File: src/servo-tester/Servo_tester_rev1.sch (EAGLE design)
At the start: 19 parts, among them IC1 7806T

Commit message: Fixed discrepancy between brd and sch, corrected pulldowns
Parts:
- added R10, R7, R8, R9: 10M, adafruit:R-US_0204/5
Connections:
- new net 33V_PULLUP: JP3.6, JP4.2, JP5.2, JP6.2, JP7.2
- net BTN1: now also R7.1
- net BTN2: now also R8.2
- net BTN3: now also R9.2
- net BTN4: now also R10.2
- net GND: now also R10.1, R7.2, R8.1, R9.1; no longer JP4.2, JP5.2, JP6.2, JP7.2
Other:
- moved on the sheet: JP4, JP5, JP6, JP7

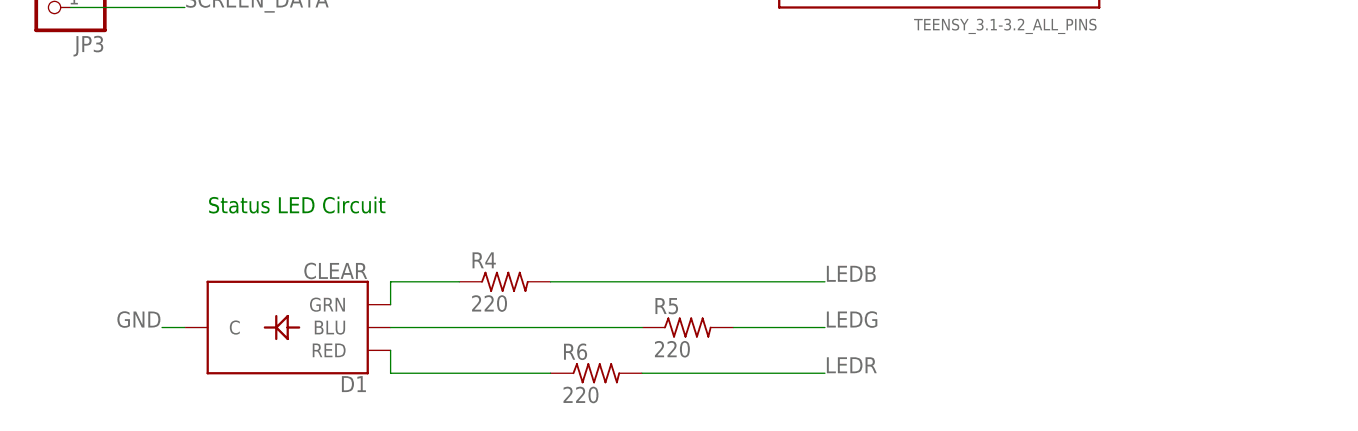
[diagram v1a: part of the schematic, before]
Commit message: fixed DRCs and made smaller
also added copper fill
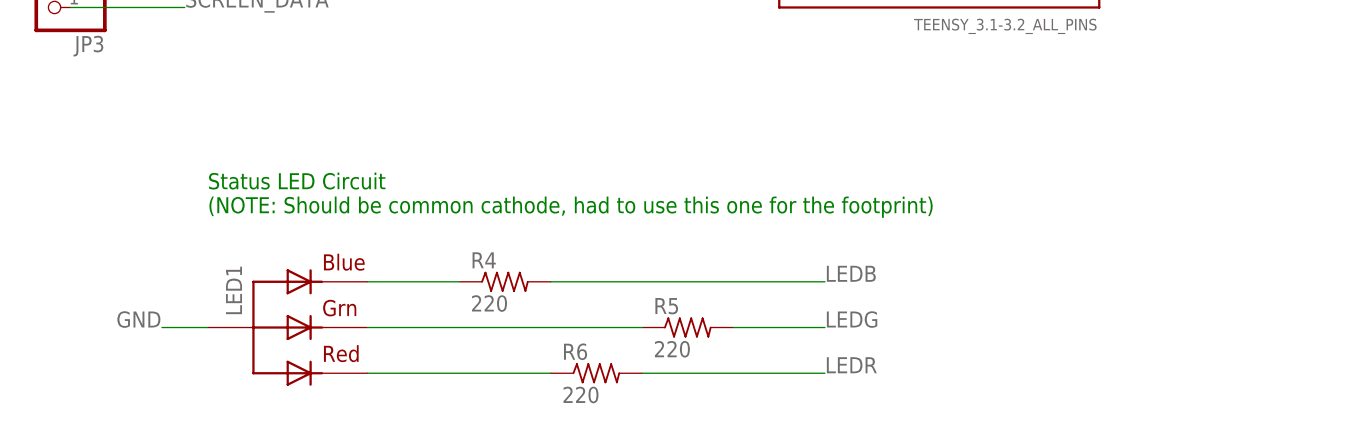
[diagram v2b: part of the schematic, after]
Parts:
- removed D1: CLEAR, SparkFun-LED:LED-RGB-CCCLEAR
- added LED1: RGBLED_CA-5MM, adafruit:RGBLED_CA-5MM
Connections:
- net GND: now also LED1.VCC; no longer D1.C
- net N$13: now also LED1.RED; no longer D1.RED
- net N$14: now also LED1.BLUE; no longer D1.GRN
- net N$15: now also LED1.GREEN; no longer D1.BLU
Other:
- note added: "Status LED Circuit (NOTE: Should be common cathode, had to use this one for the footprint)"
- note removed: "Status LED Circuit"
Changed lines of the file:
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@@
 <classes>
 <class number="0" name="default" width="0" drill="0">
+<clearance class="0" value="0.205"/>
 </class>
 </classes>
@@
 <part name="C2" library="adafruit" library_urn="urn:adsk.eagle:library:420" deviceset="C-US" device="050-024X044" package3d_urn="urn:adsk.eagle:package:6240356/1"/>
 <part name="C3" library="adafruit" library_urn="urn:adsk.eagle:library:420" deviceset="C-US" device="050-024X044" package3d_urn="urn:adsk.eagle:package:6240356/1" value="0.1u"/>
-<part name="D1" library="SparkFun-LED" library_urn="urn:adsk.eagle:library:529" deviceset="LED-RGB-CC" device="CLEAR" package3d_urn="urn:adsk.eagle:package:39368/1" value="CLEAR"/>
 <part name="JP4" library="microbuilder" deviceset="HEADER-1X2" device="ROUND"/>
 <part name="JP5" library="microbuilder" deviceset="HEADER-1X2" device="ROUND"/>
@@
 <part name="R9" library="adafruit" library_urn="urn:adsk.eagle:library:420" deviceset="R-US_" device="0204/5" package3d_urn="urn:adsk.eagle:package:6240595/1" value="10M"/>
 <part name="R10" library="adafruit" library_urn="urn:adsk.eagle:library:420" deviceset="R-US_" device="0204/5" package3d_urn="urn:adsk.eagle:package:6240595/1" value="10M"/>
+<part name="LED1" library="adafruit" library_urn="urn:adsk.eagle:library:420" deviceset="RGBLED_CA" device="-5MM" package3d_urn="urn:adsk.eagle:package:6240652/1"/>
 </parts>
 <sheets>
@@
 <text x="198.12" y="121.92" size="1.778" layer="91">Voltage Stepdown</text>
 <text x="218.44" y="76.2" size="1.778" layer="91">Servo Connector</text>
-<text x="63.5" y="27.94" size="1.778" layer="91">Status LED Circuit</text>
+<text x="63.5" y="27.94" size="1.778" layer="91">Status LED Circuit
+(NOTE: Should be common cathode, had to use this one for the footprint)</text>
 <text x="25.4" y="76.2" size="1.778" layer="91">Screen Connector</text>
 <text x="35.56" y="137.16" size="1.778" layer="91">Buttons</text>
@@
 <attribute name="VALUE" x="138.811" y="161.036" size="1.778" layer="96" rot="R180"/>
 </instance>
-<instance part="D1" gate="G$1" x="73.66" y="15.24" smashed="yes" rot="R180">
-<attribute name="NAME" x="81.28" y="9.8425" size="1.778" layer="95" font="vector" rot="R180"/>
-<attribute name="VALUE" x="81.28" y="20.6375" size="1.778" layer="95" font="vector" rot="R180" align="top-left"/>
-</instance>
 <instance part="JP4" gate="G$1" x="45.72" y="127" smashed="yes" rot="R270">
 <attribute name="NAME" x="51.435" y="133.35" size="1.778" layer="95"/>
@@
 <attribute name="NAME" x="77.47" y="97.5614" size="1.778" layer="95" rot="R180"/>
 <attribute name="VALUE" x="77.47" y="102.362" size="1.778" layer="96" rot="R180"/>
+</instance>
+<instance part="LED1" gate="G$1" x="73.66" y="15.24" smashed="yes">
+<attribute name="NAME" x="67.31" y="16.51" size="1.778" layer="95" rot="R90"/>
 </instance>
 </instances>
@@
 </segment>
 <segment>
-<wire x1="60.96" y1="15.24" x2="58.42" y2="15.24" width="0.1524" layer="91"/>
 <label x="53.34" y="15.24" size="1.778" layer="95"/>
-<pinref part="D1" gate="G$1" pin="C"/>
+<pinref part="LED1" gate="G$1" pin="VCC"/>
+<wire x1="58.42" y1="15.24" x2="63.5" y2="15.24" width="0.1524" layer="91"/>
 </segment>
 <segment>
@@
 <net name="N$13" class="0">
 <segment>
-<wire x1="101.6" y1="10.16" x2="83.82" y2="10.16" width="0.1524" layer="91"/>
+<wire x1="101.6" y1="10.16" x2="81.28" y2="10.16" width="0.1524" layer="91"/>
 <pinref part="R6" gate="G$1" pin="1"/>
-<pinref part="D1" gate="G$1" pin="RED"/>
-<wire x1="83.82" y1="10.16" x2="83.82" y2="12.7" width="0.1524" layer="91"/>
+<pinref part="LED1" gate="G$1" pin="RED"/>
 </segment>
 </net>
 <net name="N$14" class="0">
 <segment>
-<wire x1="83.82" y1="20.32" x2="91.44" y2="20.32" width="0.1524" layer="91"/>
+<wire x1="81.28" y1="20.32" x2="91.44" y2="20.32" width="0.1524" layer="91"/>
 <pinref part="R4" gate="G$1" pin="1"/>
-<pinref part="D1" gate="G$1" pin="GRN"/>
-<wire x1="83.82" y1="20.32" x2="83.82" y2="17.78" width="0.1524" layer="91"/>
+<pinref part="LED1" gate="G$1" pin="BLUE"/>
 </segment>
 </net>
 <net name="N$15" class="0">
 <segment>
-<wire x1="83.82" y1="15.24" x2="111.76" y2="15.24" width="0.1524" layer="91"/>
+<wire x1="81.28" y1="15.24" x2="111.76" y2="15.24" width="0.1524" layer="91"/>
 <pinref part="R5" gate="G$1" pin="1"/>
-<pinref part="D1" gate="G$1" pin="BLU"/>
-</segment>
-</net>
+<pinref part="LED1" gate="G$1" pin="GREEN"/>
+</segment>
+</net>

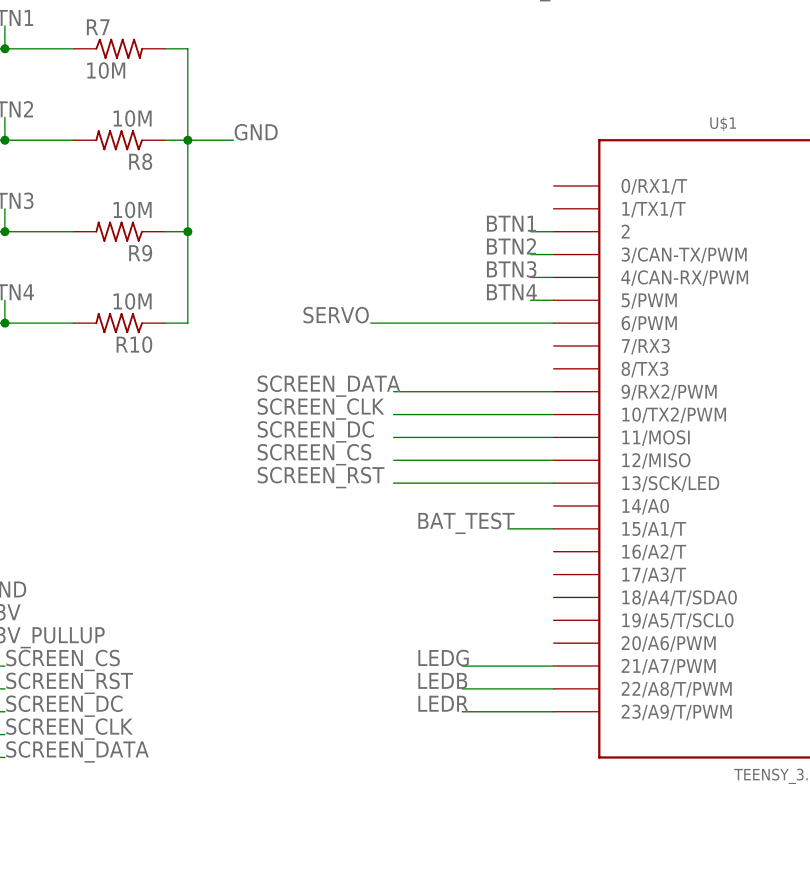
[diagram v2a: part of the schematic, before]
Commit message: Moved led to unblock usb port, tidied up buttons
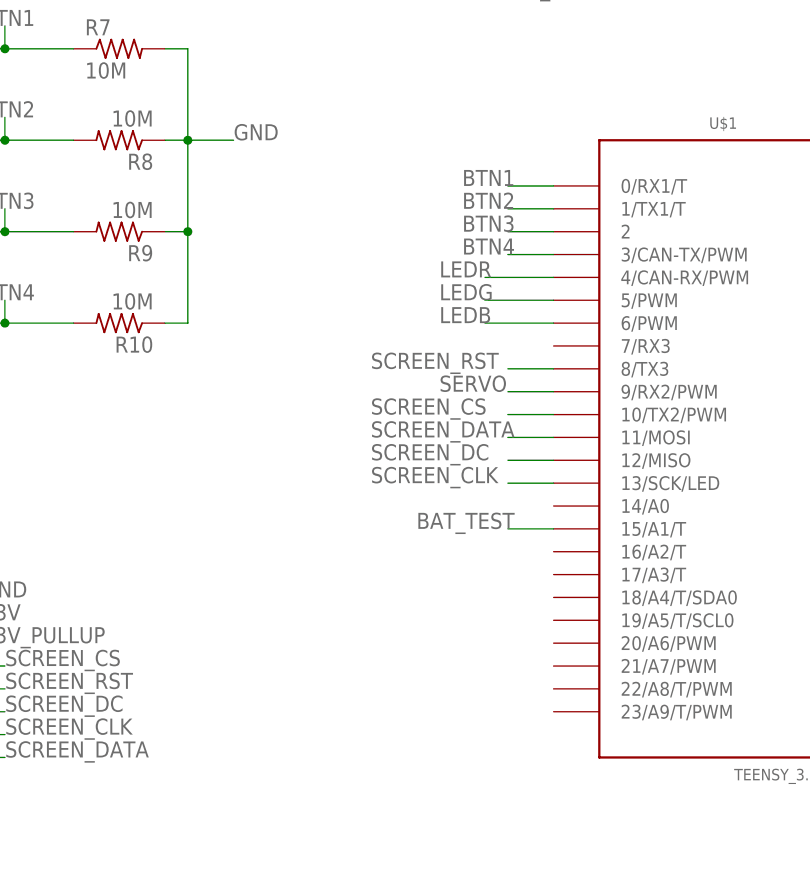
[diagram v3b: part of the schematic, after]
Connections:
- net BTN1: now also U$1.0/RX1/T; no longer U$1.2
- net BTN2: now also U$1.1/TX1/T; no longer U$1.3/CAN-TX/PWM
- net BTN3: now also U$1.2; no longer U$1.4/CAN-RX/PWM
- net BTN4: now also U$1.3/CAN-TX/PWM; no longer U$1.5/PWM
- net LEDB: now also U$1.6/PWM; no longer U$1.22/A8/T/PWM
- net LEDG: now also U$1.5/PWM; no longer U$1.21/A7/PWM
- net LEDR: now also U$1.4/CAN-RX/PWM; no longer U$1.23/A9/T/PWM
- net SCREEN_CLK: now also U$1.13/SCK/LED; no longer U$1.10/TX2/PWM
- net SCREEN_CS: now also U$1.10/TX2/PWM; no longer U$1.12/MISO
- net SCREEN_DATA: now also U$1.11/MOSI; no longer U$1.9/RX2/PWM
- net SCREEN_DC: now also U$1.12/MISO; no longer U$1.11/MOSI
- net SCREEN_RST: now also U$1.8/TX3; no longer U$1.13/SCK/LED
- net SERVO: now also U$1.9/RX2/PWM; no longer U$1.6/PWM
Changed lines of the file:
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@@
 <?xml version="1.0" encoding="utf-8"?>
 <!DOCTYPE eagle SYSTEM "eagle.dtd">
-<eagle version="9.5.1">
+<eagle version="9.5.2">
 <drawing>
 <settings>
@@
 <net name="BTN2" class="0">
 <segment>
-<pinref part="U$1" gate="G$1" pin="3/CAN-TX/PWM"/>
-<wire x1="119.38" y1="106.68" x2="121.92" y2="106.68" width="0.1524" layer="91"/>
-<label x="114.3" y="106.68" size="1.778" layer="95"/>
-</segment>
-<segment>
 <label x="58.42" y="121.92" size="1.778" layer="95"/>
 <pinref part="JP5" gate="G$1" pin="1"/>
@@
 <junction x="60.96" y="119.38"/>
 </segment>
+<segment>
+<pinref part="U$1" gate="G$1" pin="1/TX1/T"/>
+<wire x1="121.92" y1="111.76" x2="116.84" y2="111.76" width="0.1524" layer="91"/>
+<label x="111.76" y="111.76" size="1.778" layer="95"/>
+</segment>
 </net>
 <net name="BTN1" class="0">
-<segment>
-<pinref part="U$1" gate="G$1" pin="2"/>
-<wire x1="119.38" y1="109.22" x2="121.92" y2="109.22" width="0.1524" layer="91"/>
-<label x="114.3" y="109.22" size="1.778" layer="95"/>
-</segment>
 <segment>
 <label x="58.42" y="132.08" size="1.778" layer="95"/>
@@
 <junction x="60.96" y="129.54"/>
 </segment>
+<segment>
+<pinref part="U$1" gate="G$1" pin="0/RX1/T"/>
+<wire x1="121.92" y1="114.3" x2="116.84" y2="114.3" width="0.1524" layer="91"/>
+<label x="111.76" y="114.3" size="1.778" layer="95"/>
+</segment>
 </net>
 <net name="BTN3" class="0">
-<segment>
-<pinref part="U$1" gate="G$1" pin="4/CAN-RX/PWM"/>
-<wire x1="119.38" y1="104.14" x2="121.92" y2="104.14" width="0.1524" layer="91"/>
-<label x="114.3" y="104.14" size="1.778" layer="95"/>
-</segment>
 <segment>
 <label x="58.42" y="111.76" size="1.778" layer="95"/>
@@
 <junction x="60.96" y="109.22"/>
 </segment>
+<segment>
+<pinref part="U$1" gate="G$1" pin="2"/>
+<wire x1="121.92" y1="109.22" x2="116.84" y2="109.22" width="0.1524" layer="91"/>
+<label x="111.76" y="109.22" size="1.778" layer="95"/>
+</segment>
 </net>
 <net name="33V" class="0">
@@
 </segment>
 <segment>
-<pinref part="U$1" gate="G$1" pin="12/MISO"/>
-<wire x1="121.92" y1="83.82" x2="104.14" y2="83.82" width="0.1524" layer="91"/>
-<label x="88.9" y="83.82" size="1.778" layer="95"/>
+<pinref part="U$1" gate="G$1" pin="10/TX2/PWM"/>
+<wire x1="121.92" y1="88.9" x2="116.84" y2="88.9" width="0.1524" layer="91"/>
+<label x="101.6" y="88.9" size="1.778" layer="95"/>
 </segment>
 </net>
@@
 </segment>
 <segment>
-<pinref part="U$1" gate="G$1" pin="13/SCK/LED"/>
-<wire x1="121.92" y1="81.28" x2="104.14" y2="81.28" width="0.1524" layer="91"/>
-<label x="88.9" y="81.28" size="1.778" layer="95"/>
+<pinref part="U$1" gate="G$1" pin="8/TX3"/>
+<wire x1="121.92" y1="93.98" x2="116.84" y2="93.98" width="0.1524" layer="91"/>
+<label x="101.6" y="93.98" size="1.778" layer="95"/>
 </segment>
 </net>
@@
 </segment>
 <segment>
-<pinref part="U$1" gate="G$1" pin="11/MOSI"/>
-<wire x1="121.92" y1="86.36" x2="104.14" y2="86.36" width="0.1524" layer="91"/>
-<label x="88.9" y="86.36" size="1.778" layer="95"/>
+<pinref part="U$1" gate="G$1" pin="12/MISO"/>
+<wire x1="121.92" y1="83.82" x2="116.84" y2="83.82" width="0.1524" layer="91"/>
+<label x="101.6" y="83.82" size="1.778" layer="95"/>
 </segment>
 </net>
@@
 </segment>
 <segment>
-<wire x1="101.6" y1="99.06" x2="121.92" y2="99.06" width="0.1524" layer="91"/>
-<label x="93.98" y="99.06" size="1.778" layer="95"/>
-<pinref part="U$1" gate="G$1" pin="6/PWM"/>
+<pinref part="U$1" gate="G$1" pin="9/RX2/PWM"/>
+<wire x1="121.92" y1="91.44" x2="116.84" y2="91.44" width="0.1524" layer="91"/>
+<label x="109.22" y="91.44" size="1.778" layer="95"/>
 </segment>
 </net>
@@
 </segment>
 <segment>
-<pinref part="U$1" gate="G$1" pin="22/A8/T/PWM"/>
-<wire x1="121.92" y1="58.42" x2="111.76" y2="58.42" width="0.1524" layer="91"/>
-<label x="106.68" y="58.42" size="1.778" layer="95"/>
+<pinref part="U$1" gate="G$1" pin="6/PWM"/>
+<wire x1="121.92" y1="99.06" x2="114.3" y2="99.06" width="0.1524" layer="91"/>
+<label x="109.22" y="99.06" size="1.778" layer="95"/>
 </segment>
 </net>
@@
 </segment>
 <segment>
-<pinref part="U$1" gate="G$1" pin="21/A7/PWM"/>
-<wire x1="121.92" y1="60.96" x2="111.76" y2="60.96" width="0.1524" layer="91"/>
-<label x="106.68" y="60.96" size="1.778" layer="95"/>
+<pinref part="U$1" gate="G$1" pin="5/PWM"/>
+<wire x1="121.92" y1="101.6" x2="114.3" y2="101.6" width="0.1524" layer="91"/>
+<label x="109.22" y="101.6" size="1.778" layer="95"/>
 </segment>
 </net>
 <net name="LEDR" class="0">
-<segment>
-<pinref part="U$1" gate="G$1" pin="23/A9/T/PWM"/>
-<wire x1="121.92" y1="55.88" x2="111.76" y2="55.88" width="0.1524" layer="91"/>
-<label x="106.68" y="55.88" size="1.778" layer="95"/>
-</segment>
 <segment>
 <wire x1="111.76" y1="10.16" x2="132.08" y2="10.16" width="0.1524" layer="91"/>
 <pinref part="R6" gate="G$1" pin="2"/>
 <label x="132.08" y="10.16" size="1.778" layer="95"/>
+</segment>
+<segment>
+<pinref part="U$1" gate="G$1" pin="4/CAN-RX/PWM"/>
+<wire x1="121.92" y1="104.14" x2="114.3" y2="104.14" width="0.1524" layer="91"/>
+<label x="109.22" y="104.14" size="1.778" layer="95"/>
 </segment>
 </net>
@@
 </segment>
 <segment>
-<pinref part="U$1" gate="G$1" pin="5/PWM"/>
-<wire x1="121.92" y1="101.6" x2="119.38" y2="101.6" width="0.1524" layer="91"/>
-<label x="114.3" y="101.6" size="1.778" layer="95"/>
+<pinref part="U$1" gate="G$1" pin="3/CAN-TX/PWM"/>
+<wire x1="121.92" y1="106.68" x2="116.84" y2="106.68" width="0.1524" layer="91"/>
+<label x="111.76" y="106.68" size="1.778" layer="95"/>
 </segment>
 </net>
@@
 </segment>
 <segment>
-<pinref part="U$1" gate="G$1" pin="10/TX2/PWM"/>
-<wire x1="121.92" y1="88.9" x2="104.14" y2="88.9" width="0.1524" layer="91"/>
-<label x="88.9" y="88.9" size="1.778" layer="95"/>
+<pinref part="U$1" gate="G$1" pin="13/SCK/LED"/>
+<wire x1="121.92" y1="81.28" x2="116.84" y2="81.28" width="0.1524" layer="91"/>
+<label x="101.6" y="81.28" size="1.778" layer="95"/>
 </segment>
 </net>
@@
 </segment>
 <segment>
-<pinref part="U$1" gate="G$1" pin="9/RX2/PWM"/>
-<wire x1="121.92" y1="91.44" x2="104.14" y2="91.44" width="0.1524" layer="91"/>
-<label x="88.9" y="91.44" size="1.778" layer="95"/>
-</segment>
-</net>
+<pinref part="U$1" gate="G$1" pin="11/MOSI"/>
+<wire x1="121.92" y1="86.36" x2="116.84" y2="86.36" width="0.1524" layer="91"/>
+<label x="101.6" y="86.36" size="1.778" layer="95"/>
+</segment>
+</net>
